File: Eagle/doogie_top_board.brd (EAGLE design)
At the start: 88.9 x 75 mm, 26 parts, among them U1 GY-521MPU6050

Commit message: Add first version of schematics
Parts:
- removed OK1, OK2, OK3, OK4, OK5, OK6, OK7: PC817, optocoupler:DIL04
- removed R10, R11, R12, R13, R14, R7, R8, R9: (no value), rcl:0204/7
- added BUZZER: F/TMB, buzzer:F/TMB
- added D1, D2: GREEN, SparkFun-LED:LED_3MM
- added D3: 1N4004, adafruit:DO41-10
- added K1: G5L, relay:G5LE
- added S1, S2: MOMENTARY-SWITCH-SPST-PTH-6.0MM, SparkFun-Switches:TACTILE_SWITCH_PTH_6.0MM
- added T1, T2: BC337, transistor:TO92
- added U2: U1V10F5, pololu:U1V10F5
- J1, J2: device SparkFun-Connectors:1X10 -> SparkFun-Connectors:1X12
- R1: value (none) -> 750R
- R2: value (none) -> 390R
- R3: value (none) -> 820R
- R4: value (none) -> 680R
- R5, R6: value (none) -> 10k
- moved R5 133.1 mm to (-50.0, -60.0), turned to 0 degrees
- moved R6 128.4 mm to (-50.0, -64.0), turned to 0 degrees
- moved R4 115.8 mm to (-50.0, -30.0), turned to 0 degrees
- moved R3 71.8 mm to (33.5, 46.3), turned to 270 degrees
- moved R2 67.8 mm to (30.9, 55.1), turned to 270 degrees
- moved J2 24.4 mm to (24.1, 34.3), turned to 90 degrees
- moved J1 24.3 mm to (-24.1, 34.3), turned to 90 degrees
- moved R1 19.4 mm to (-38.8, 32.3), flipped to the bottom, turned to 0 degrees
- moved U1 2.54 mm to (-1.27, 67.3)
- moved U$2 1.48 mm to (-32.5, 0.00)
- moved U$3 1.27 mm to (-1.27, 43.2)
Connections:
- removed net GPIO_H-BRIDGE_!STDBY: R4.1
- removed net GPIO_MOTOR_LEFT_EN1: R2.1
- removed net GPIO_MOTOR_LEFT_EN2: R3.1
- removed net GPIO_MOTOR_LEFT_PWM: R1.1
- removed net GPIO_MOTOR_RIGHT_EN1: R6.1
- removed net GPIO_MOTOR_RIGHT_EN2: R7.1
- removed net GPIO_MOTOR_RIGHT_PWM: R5.1
- removed net VCC: R10.2, R11.2, R12.2, R13.2, R14.2, R8.2, R9.2
- new net 5V: BUZZER.+, D3.C, K1.1, U$2.2, U$2.4, U2.VOUT
- new net ADC_A0_CHANNEL: K1.P, U$3.7
- new net BATT_MONITORING_EN: U$2.23
- new net BUZZER_CTRL: R1.1, R4.1, U$2.19
- new net GND@7: U$2.14, U$2.20, U$2.30, U$2.34, U$2.6
- new net LEFT_RCVR_EN: U$2.21
- new net N$8: R4.2, T2.2
- new net N$9: K1.S, R5.1, R6.2
- new net VOUT: J2.10, R3.2
- net 3.3V: now also J2.12; no longer OK1.3, OK2.3, OK3.3, OK4.3, OK5.3, OK6.3, OK7.3
- net GND: now also D1.K, D2.K, J1.1, J1.2, R6.1, S1.1, S2.1, T1.1, T2.1, U$2.25, U$2.39, U$2.9, U2.GND; no longer OK1.2, OK2.2, OK3.2, OK4.2, OK5.2, OK6.2, OK7.2
- net H-BRIDGE_!STDBY: now also J1.7, U$2.11; no longer J1.6, OK4.4, R11.1
- net LEFT_FRONT_EMITTER: now also J1.11, U$2.15; no longer J1.2
- net LEFT_FRONT_RCVR: now also J1.12; no longer J1.1
- net LEFT_RCVR: now also J1.5, K1.O; no longer J1.8, U$3.7
- net LEFT_RIGHT_EMITTER: now also J1.6, J2.4, U$2.10; no longer J1.7, J2.7
- net MOTOR_LEFT_EN1: now also J1.9, U$2.13; no longer J1.4, OK2.4, R9.1
- net MOTOR_LEFT_EN2: now also J1.8, U$2.12; no longer J1.5, OK3.4, R10.1
- net MOTOR_LEFT_ENCA: now also J1.4, U$2.8; no longer J1.9
- net MOTOR_LEFT_ENCB: now also J1.3, U$2.7; no longer J1.10
- net MOTOR_LEFT_PWM: now also J1.10, U$2.35; no longer J1.3, OK1.4, R8.1
- net MOTOR_RIGHT_EN1: now also J2.6, U$2.36; no longer J2.4, OK6.4, R13.1
- net MOTOR_RIGHT_EN2: now also U$2.37; no longer OK7.4, R14.1
- net MOTOR_RIGHT_ENCA: now also J2.2, U$2.38; no longer J2.9
- net MOTOR_RIGHT_ENCB: now also J2.1, U$2.40; no longer J2.10
- net MOTOR_RIGHT_PWM: now also J2.7, U$2.32; no longer J2.3, OK5.4, R12.1
- net N$1: now also BUZZER.-, T1.3; no longer OK6.1, R6.2
- net N$2: now also R1.2, T1.2; no longer OK7.1, R7.2
- net N$3: now also S2.3, U$2.33; no longer OK5.1, R5.2
- net N$4: now also S1.3, U$2.31; no longer OK4.1, R4.2
- net N$5: now also D1.A, R2.1; no longer OK2.1, R2.2
- net N$6: now also D2.A, R3.1; no longer OK3.1, R3.2
- net N$7: now also D3.A, K1.2, T2.3; no longer OK1.1, R1.2
- net RIGHT_FRONT_EMITTER: now also J2.8, U$2.28; no longer J2.2
- net RIGHT_FRONT_RCVR: now also J2.9; no longer J2.1
- net RIGHT_RCVR: now also J2.3; no longer J2.8
- net V_BATT: now also J2.11, R2.2, R5.2, U2.VIN; no longer U$2.2, U$2.4
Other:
- board size 88.9 x 75 mm -> 92.9 x 75 mm

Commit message: Route bottom board
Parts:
- removed D3: 1N4004, adafruit:DO41-10
- removed K1: G5L, relay:G5LE
- removed R4: 680R, rcl:0204/7
- removed T2: BC337, transistor:TO92
- added U3: 74HC4051_SPARKFUN, doogie:74HC4051_SPARKFUN
- moved R5 99.0 mm to (18.0, 12.0), turned to 90 degrees
- moved R6 98.7 mm to (13.0, 12.0), turned to 270 degrees
- moved U2 28.2 mm to (27.0, 14.3)
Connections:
- net LEFT_FRONT_EMITTER renamed FRONT_EMITTERS_CTRL
- removed net BATT_MONITORING_EN: U$2.23
- removed net LEFT_RCVR_EN: U$2.21
- removed net LEFT_RIGHT_EMITTER: J1.6, J2.4, U$2.10
- removed net N$7: D3.A, K1.2, T2.3
- removed net N$8: R4.2, T2.2
- removed net RIGHT_FRONT_EMITTER: J2.8, U$2.28
- new net ADC_A0_CHANNEL_CTRL: U$2.21, U3.S0
- new net LEFT_EMITTER_CTRL: J1.1, U$2.10
- new net RIGHT_EMITTER_CTRL: J2.3, U$2.28
- net 3.3V: now also U3.VCC, U3.VCC@1
- net 5V: no longer D3.C, K1.1
- net ADC_A0_CHANNEL: now also U3.Z; no longer K1.P
- net BUZZER_CTRL: no longer R4.1
- net GND: now also J1.6, U3.GND, U3.GND@1, U3.S1, U3.S2, U3.VEE, U3.VEE@1; no longer J1.1, T2.1
- net LEFT_RCVR: now also U3.Y0; no longer K1.O
- net N$9: now also U3.Y1; no longer K1.S
- net RIGHT_RCVR: now also J2.4; no longer J2.3

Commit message: Make top board routing sketch
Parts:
- added D3: 1N4004, diode:DO41-10
- U$2: device RPI-Zero:RASPBERRYPI_BASTELSTUBE_V13_RASPI_BOARD_B+_FULL -> doogie:RASPBERRYPI_BASTELSTUBE_V13_RASPI_BOARD_B+_FULL
- moved U2 46.5 mm to (-19.4, 12.7)
- moved BUZZER 8.60 mm to (-34.5, 53.7)
- moved U3 6.94 mm to (1.40, 12.7), turned to 270 degrees
- moved R6 5.59 mm to (18.5, 12.7), turned to 90 degrees
- moved R5 4.28 mm to (22.2, 12.7), turned to 270 degrees
- moved J1 3.03 mm to (-23.1, 31.4)
- moved J2 3.03 mm to (23.1, 31.4)
- moved T1 1.82 mm to (-40.6, 37.2), flipped to the top
- moved R1 1.81 mm to (-40.6, 32.3), flipped to the top, turned to 180 degrees
- moved U$3 1.27 mm to (0.00, 43.2)
- moved U1 1.27 mm to (0.00, 67.3)
- moved D2 0.09 mm to (39.4, 53.3)
- moved R3 0.06 mm to (33.5, 46.2)
- moved R2 0.06 mm to (31.0, 55.1)
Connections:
- removed net GND@7: U$2.14, U$2.20, U$2.30, U$2.34, U$2.6
- net 5V: now also D3.C
- net GND: now also J1.10, J2.8, S1.3, S2.3, U$2.14, U$2.20, U$2.30, U$2.34, U$2.6; no longer J1.6, S1.1, S2.1
- net H-BRIDGE_!STDBY: now also J1.9, U$2.13; no longer J1.7, U$2.11
- net LEFT_EMITTER_CTRL: now also U$2.7; no longer U$2.10
- net MOTOR_LEFT_EN1: now also J1.8, U$2.12; no longer J1.9, U$2.13
- net MOTOR_LEFT_EN2: now also J1.7, U$2.11; no longer J1.8, U$2.12
- net MOTOR_LEFT_ENCA: now also J1.3; no longer J1.4
- net MOTOR_LEFT_ENCB: now also J1.4, U$2.10; no longer J1.3, U$2.7
- net MOTOR_LEFT_PWM: now also J1.6; no longer J1.10
- net MOTOR_RIGHT_EN1: now also J2.7, U$2.29; no longer J2.6, U$2.36
- net MOTOR_RIGHT_EN2: now also J2.6, U$2.31; no longer J2.5, U$2.37
- net MOTOR_RIGHT_ENCA: now also U$2.36; no longer U$2.38
- net MOTOR_RIGHT_ENCB: now also U$2.38; no longer U$2.40
- net MOTOR_RIGHT_PWM: now also J2.5; no longer J2.7
- net N$1: now also D3.A
- net N$3: now also S2.1, U$2.37; no longer S2.3, U$2.33
- net N$4: now also S1.1, U$2.40; no longer S1.3, U$2.31
- net RIGHT_EMITTER_CTRL: now also U$2.33; no longer U$2.28
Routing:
- net LEFT_RCVR: track 0.00 -> 75.6 mm, vias 0 -> 2
- net MOTOR_LEFT_PWM: track 0.00 -> 73.0 mm, vias 0 -> 2
- net I2C_SCL: track 0.00 -> 55.9 mm
- net I2C_SDA: track 0.00 -> 54.8 mm
- net BUZZER_CTRL: track 0.00 -> 43.8 mm, vias 0 -> 2
- net LEFT_FRONT_RCVR: track 0.00 -> 43.4 mm
- net FRONT_EMITTERS_CTRL: track 0.00 -> 38.8 mm
- net H-BRIDGE_!STDBY: track 0.00 -> 31.5 mm
- net MOTOR_RIGHT_EN1: track 0.00 -> 28.6 mm
- net MOTOR_LEFT_EN2: track 0.00 -> 27.3 mm
- net MOTOR_LEFT_EN1: track 0.00 -> 25.4 mm
- net N$9: track 0.00 -> 25.2 mm
- net MOTOR_RIGHT_EN2: track 0.00 -> 24.8 mm
- net RIGHT_FRONT_RCVR: track 0.00 -> 20.8 mm
- net ADC_A0_CHANNEL: track 0.00 -> 20.0 mm
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
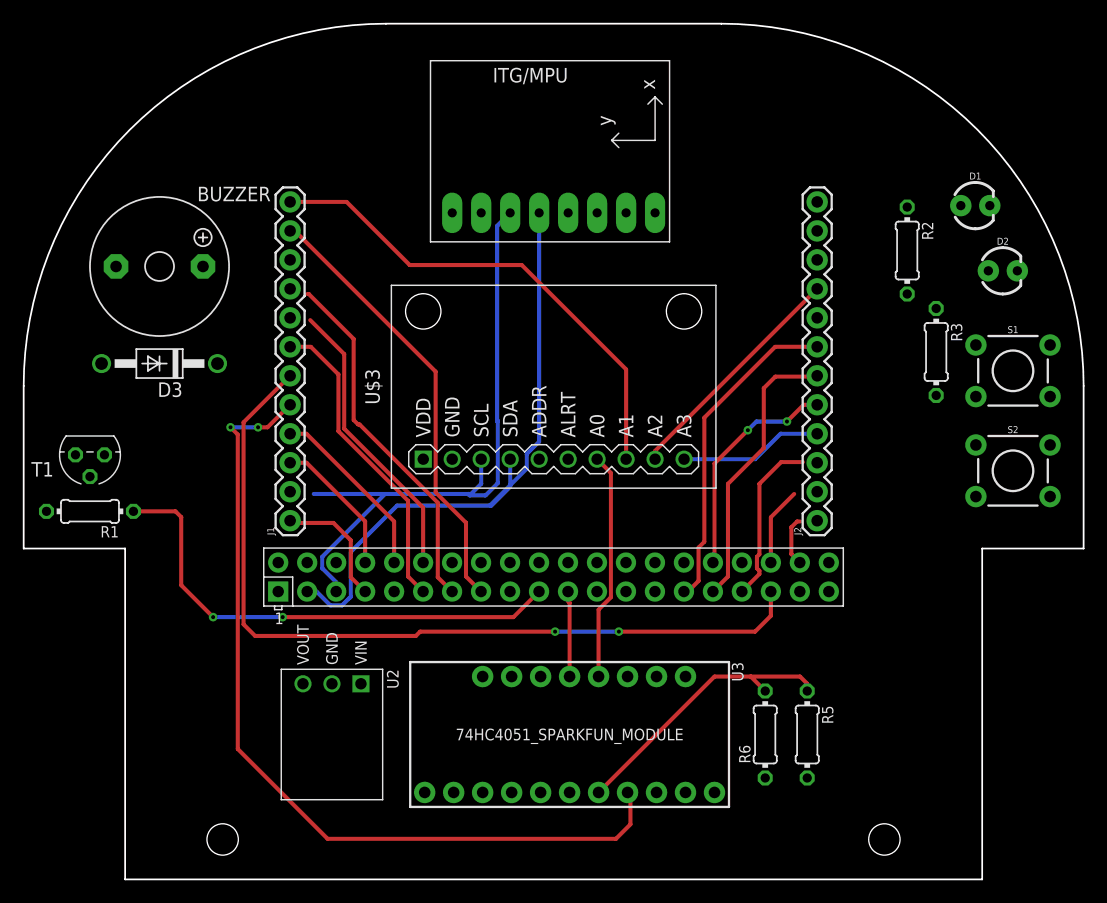
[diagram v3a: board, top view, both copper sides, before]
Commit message: Add first step of top board routing
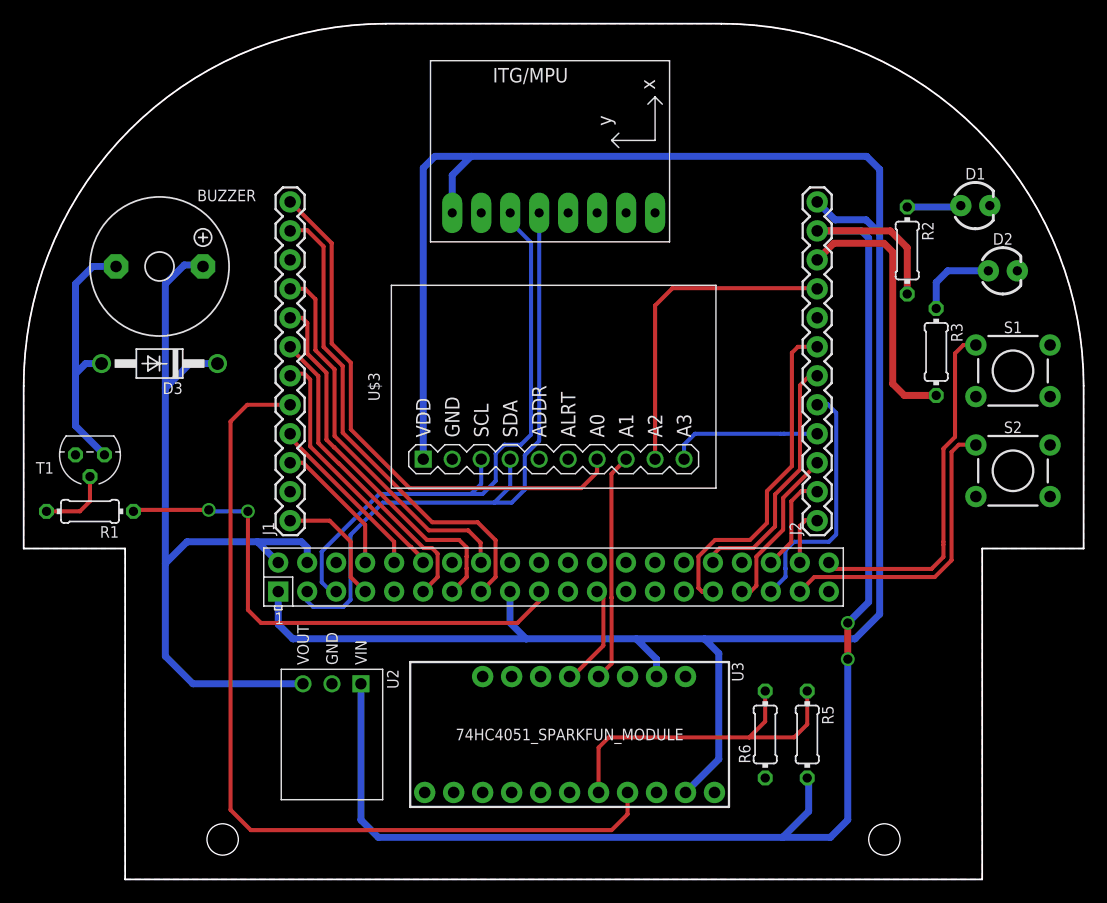
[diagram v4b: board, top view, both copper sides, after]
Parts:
- U$3: device diy-modules:ADC-4CH-ADS1115 -> doogie:ADC-4CH-ADS1115
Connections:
- removed net ADC_A0_CHANNEL: U$3.7, U3.Z
- removed net ADC_A0_CHANNEL_CTRL: U$2.21, U3.S0
- new net ADC_A1_CHANNEL: U$3.8, U3.Z
- new net ADC_A1_CHANNEL_CTRL: U$2.23, U3.S0
- net H-BRIDGE_!STDBY: now also U$2.16; no longer U$2.13
- net LEFT_FRONT_RCVR: now also U$3.7; no longer U$3.8
- net MOTOR_LEFT_EN1: now also U$2.13; no longer U$2.12
- net MOTOR_LEFT_PWM: now also U$2.12; no longer U$2.35
- net MOTOR_RIGHT_EN1: now also U$2.31; no longer U$2.29
- net MOTOR_RIGHT_EN2: now also U$2.32; no longer U$2.31
- net MOTOR_RIGHT_PWM: now also U$2.35; no longer U$2.32
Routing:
- net 3.3V: track 0.00 -> 198.7 mm
- net V_BATT: track 0.00 -> 131.2 mm, vias 0 -> 2
- net 5V: track 0.00 -> 72.5 mm
- net MOTOR_LEFT_PWM: track 73.0 -> 22.2 mm, vias 2 -> 0
- net N$4: track 0.00 -> 31.1 mm
- net N$3: track 0.00 -> 26.3 mm
- net VOUT: track 0.00 -> 23.3 mm
- net N$1: track 0.00 -> 22.9 mm
- net ADC_A1_CHANNEL: track 0.00 -> 20.1 mm
- net ADC_A0_CHANNEL: track 20.0 -> 0.00 mm
- net ADC_A1_CHANNEL_CTRL: track 0.00 -> 9.06 mm
- net MOTOR_LEFT_EN1: track 25.4 -> 33.2 mm
- net RIGHT_FRONT_RCVR: track 20.8 -> 28.3 mm
- net ADC_A0_CHANNEL_CTRL: track 7.51 -> 0.00 mm
- net N$6: track 0.00 -> 7.28 mm
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- added copper zone on layer 1, net GND
- added copper zone on layer 16, net GND

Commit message: Add silk
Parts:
- removed U$2: RPI-ZERO, doogie:RASPBERRYPI_BASTELSTUBE_V13_RASPI_BOARD_B+_FULL
- added U5: 74HC4051_SPARKFUN, doogie:74HC4051_SPARKFUN
- U1: value GY-521MPU6050 -> RPI-ZERO; device gy-521:GY-521 -> doogie:RASPBERRYPI_BASTELSTUBE_V13_RASPI_BOARD_B+_FULL
- U3: value 74HC4051_SPARKFUN -> GY-521MPU6050; device doogie:74HC4051_SPARKFUN -> doogie:GY-521
- moved U1 74.8 mm to (-32.5, 0.00), turned to 0 degrees
- moved U3 54.6 mm to (0.00, 67.3), turned to 90 degrees
- renumbered U$3 to U4
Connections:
- net 3.3V: now also U1.1, U1.17, U5.VCC, U5.VCC@1; no longer U$2.1, U$2.17, U1.VCC, U3.VCC@1
- net 5V: now also U1.2, U1.4; no longer U$2.2, U$2.4
- net ADC_A1_CHANNEL: now also U5.Z; no longer U3.Z
- net ADC_A1_CHANNEL_CTRL: now also U1.23, U5.S0; no longer U$2.23, U3.S0
- net BUZZER_CTRL: now also U1.19; no longer U$2.19
- net FRONT_EMITTERS_CTRL: now also U1.15; no longer U$2.15
- net GND: now also U1.14, U1.20, U1.25, U1.30, U1.34, U1.39, U1.6, U1.9, U5.GND, U5.GND@1, U5.S1, U5.S2, U5.VEE, U5.VEE@1; no longer U$2.14, U$2.20, U$2.25, U$2.30, U$2.34, U$2.39, U$2.6, U$2.9, U1.GND, U3.GND@1, U3.S1, U3.S2, U3.VEE, U3.VEE@1
- net H-BRIDGE_!STDBY: now also U1.16; no longer U$2.16
- net I2C_SCL: now also U1.5, U3.SCL; no longer U$2.5, U1.SCL
- net I2C_SDA: now also U1.3, U3.SDA; no longer U$2.3, U1.SDA
- net LEFT_EMITTER_CTRL: now also U1.7; no longer U$2.7
- net LEFT_RCVR: now also U5.Y0; no longer U3.Y0
- net MOTOR_LEFT_EN1: now also U1.13; no longer U$2.13
- net MOTOR_LEFT_EN2: now also U1.11; no longer U$2.11
- net MOTOR_LEFT_ENCA: now also U1.8; no longer U$2.8
- net MOTOR_LEFT_ENCB: now also U1.10; no longer U$2.10
- net MOTOR_LEFT_PWM: now also U1.12; no longer U$2.12
- net MOTOR_RIGHT_EN1: now also U1.31; no longer U$2.31
- net MOTOR_RIGHT_EN2: now also U1.32; no longer U$2.32
- net MOTOR_RIGHT_ENCA: now also U1.36; no longer U$2.36
- net MOTOR_RIGHT_ENCB: now also U1.38; no longer U$2.38
- net MOTOR_RIGHT_PWM: now also U1.35; no longer U$2.35
- net N$3: now also U1.37; no longer U$2.37
- net N$4: now also U1.40; no longer U$2.40
- net N$9: now also U5.Y1; no longer U3.Y1
- net RIGHT_EMITTER_CTRL: now also U1.33; no longer U$2.33
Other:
- board text added: "/home/menezes/Pictures/BIR - logo (PB).bmp"
- board text added: "BUTTON 1"
- board text added: "BUTTON 2"
- board text added: "DOOGIE MOUSE"
- board text added: "v1.0.0"
